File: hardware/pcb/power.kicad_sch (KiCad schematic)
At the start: 74 parts, among them J1 XT30PW-F, J12 Solar, J13 USB-C, Q3 AO3407, Q4 BSS123, Q5 AO3407, U1 AP63203WU, U11 USBLC6, U12 IP2326, U7 CN3722, U8 MT3608B

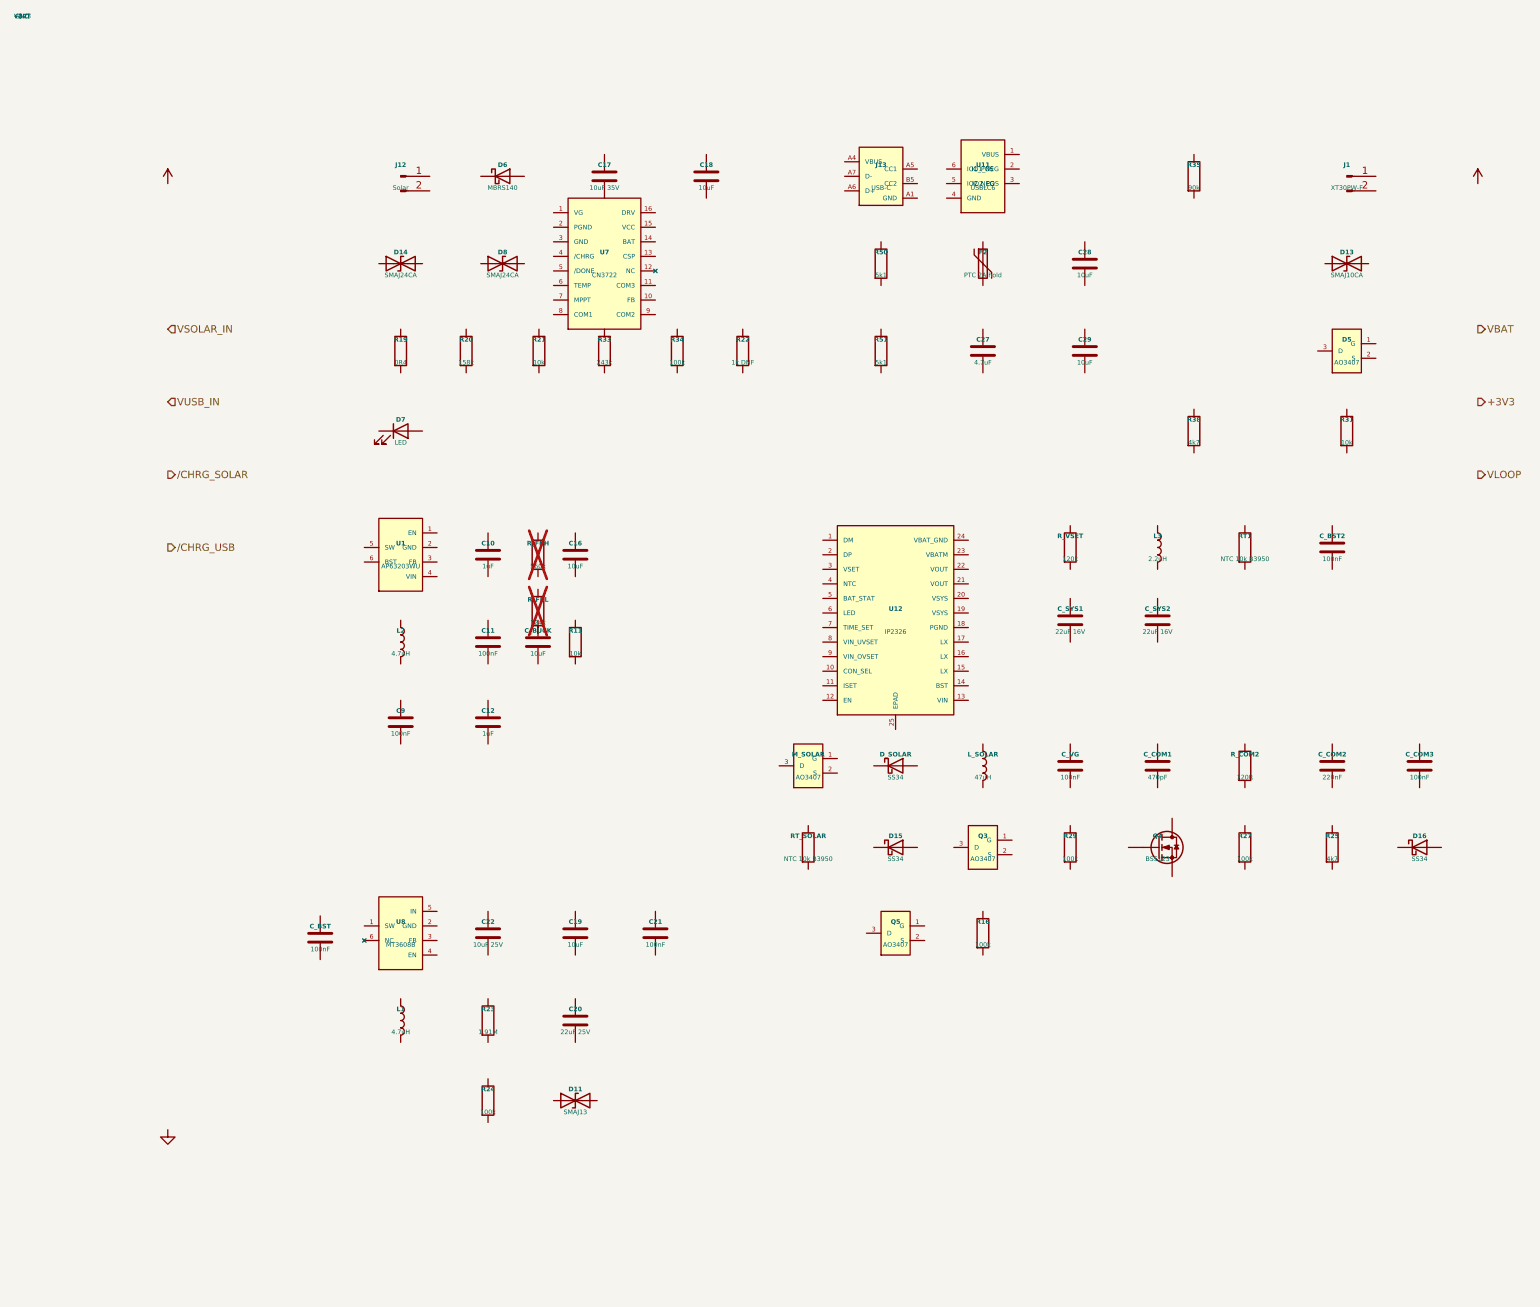
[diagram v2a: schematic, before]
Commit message: hw(pcb): wiring pass — schematic fully wired, netlist machine-verified (0 mismatches)
All four sheets wired with stub+label connectivity (434 wires, 21
explicit no-connects, PWR_FLAGs on undriven rails): power rails on
global labels, cross-sheet signals on hierarchical labels + rebuilt
top-sheet pins (24 hierarchical nets; vestigial ADC_CH* pins deleted,
GPIO14_LED corrected to the mcu-local net it really is), sheet-local
nets on local labels.

Verification (kicad-cli for the KiCad-10 format is not installable
here): hardware/pcb/kicad_wire_script.py generates the connectivity
from an embedded intent table derived from schematic_connections.md;
hardware/pcb/netlist_check.py independently re-extracts pin->net
geometrically (union-find over wires/labels/sheet pins) and diffs —
395 pins, 77 nets, 0 mismatches (output committed). Native KiCad 10
ERC + resave queued for the first interactive open.

Notable resolutions (recorded as design change #17): AP63203 FB tied
to +3V3 with the DNP divider floated at its midpoint; MT3608B pin 6
etype relaxed to passive so C_BST wiring is ERC-legal; IP2326 DM/DP
floated with no-connects (adapter detection is a two-wire future
change); D11 oriented cathode-to-VLOOP; decorative corner power
symbols replaced with real rail connectivity.

placement_constraints.md: Group G rewritten for the IP2326 hot loop,
new Group L for the CN3722 external buck (Kelvin CSP/BAT pair).
Top remaining risk flagged in blockers: AP63203 BST is NC per the
wiring doc but the AP6320x family likely requires a BST-SW cap —
resolve before layout freeze.

Co-Authored-By: Claude Fable 5 <noreply@anthropic.com>
Claude-Session: https://claude.ai/code/session_01VtMFY5Q94iYbsNPpLcPJyK
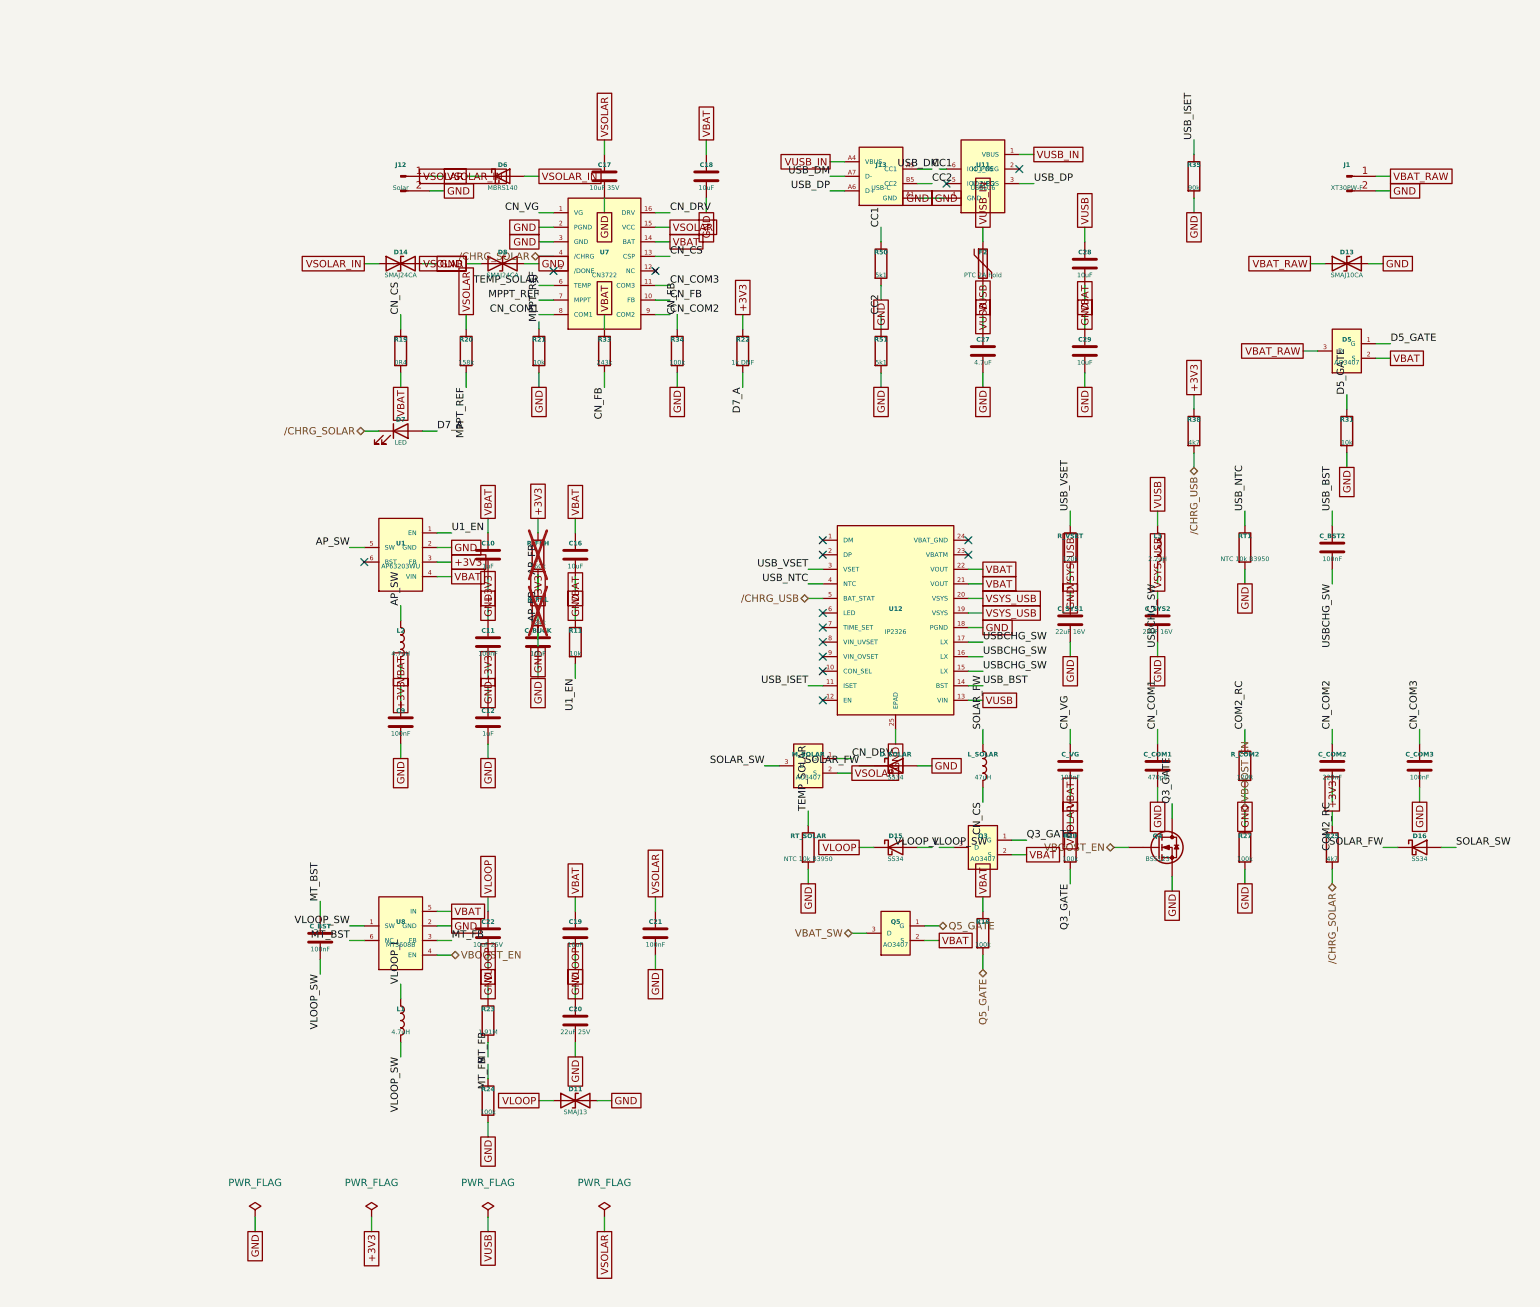
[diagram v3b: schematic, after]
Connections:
- net +3V3: now also C11.1, C12.1, C_BUCK.1, L2.2, R22.1, R25.1, R38.1, R_FBH.1, U1.3 (FB)
- net /CHRG_SOLAR: now also D7.1 (K), R25.2, U7.4 (/CHRG)
- net /CHRG_USB: now also R38.2, U12.5 (BAT_STAT)
- net GND: now also C10.2, C11.2, C12.2, C16.2, C17.2, C18.2, C19.2, C20.2, C21.2, C22.2, C27.2, C28.2, C29.2, C9.2, C_BUCK.2, C_COM1.2, C_COM3.2, C_SYS1.2, C_SYS2.2, D11.2 (A2), D13.2 (A2), D14.2 (A2), D8.2 (A2), D_SOLAR.2 (A), J1.2 (Pin_2), J12.2 (Pin_2), J13.A1 (GND), Q4.S, R21.2, R24.2, R27.2, R31.2, R34.2, R35.2, R50.2, R51.2, RT1.2, RT_SOLAR.2, R_COM2.2, R_FBL.2, R_VSET.2, U1.2 (GND), U11.4 (GND), U12.18 (PGND), U12.25 (EPAD), U7.2 (PGND), U7.3 (GND), U8.2 (GND)
- net VBAT: now also C10.1, C16.1, C18.1, C19.1, C29.1, C9.1, D5.2 (S), Q3.2 (S), Q5.2 (S), R11.1, R16.1, R19.2, R29.1, R33.1, U1.4 (VIN), U12.21 (VOUT), U12.22 (VOUT), U7.14 (BAT), U8.5 (IN)
- net VLOOP: now also C20.1, C22.1, D11.1 (A1), D15.1 (K), R23.1
- net VSOLAR_IN: now also D14.1 (A1), D6.2 (A), J12.1 (Pin_1)
- net VUSB_IN: now also F2.1, J13.A4 (VBUS), U11.1 (VBUS)
- net AP_SW: now reaches L2.1
- net AP_SW: now also U1.5 (SW)
- net CN_FB: now reaches R34.1
- net CN_FB: now also R33.2, U7.10 (FB)
- net MT_FB: now reaches R24.1
- net MT_FB: now also R23.2, U8.3 (FB)
- net VLOOP_SW: now reaches D15.2 (A)
- net VLOOP_SW: now also C_BST.2, L1.2, U8.1 (SW)
- net VUSB: now reaches C28.1
- net VUSB: now also C27.1, F2.2, L3.1, U12.13 (VIN)
- net TEMP_SOLAR: now reaches RT_SOLAR.1
- net TEMP_SOLAR: now also U7.6 (TEMP)
- net VBOOST_EN: now reaches U8.4 (EN)
- net VBOOST_EN: now also Q4.G, R27.1
- net MT_BST: now reaches U8.6 (NC)
- net MT_BST: now also C_BST.1
- net USBCHG_SW: now reaches L3.2
- net USBCHG_SW: now also C_BST2.2, U12.15 (LX), U12.16 (LX), U12.17 (LX)
- net VSOLAR: now reaches R20.1
- net VSOLAR: now also C17.1, C21.1, C_VG.2, D6.1 (K), D8.1 (A1), M_SOLAR.2 (S), U7.15 (VCC)
- net MPPT_REF: now reaches R20.2
- net MPPT_REF: now also R21.1, U7.7 (MPPT)
- net VLOOP_L: now reaches L1.1
- net VLOOP_L: now also Q3.3 (D)
- net USB_NTC: now reaches RT1.1
- net USB_NTC: now also U12.4 (NTC)
- net VSYS_USB: now reaches C_SYS2.1
- net VSYS_USB: now also C_SYS1.1, U12.19 (VSYS), U12.20 (VSYS)
- net USB_ISET: now reaches R35.1
- net USB_ISET: now also U12.11 (ISET)
- net CC2: now reaches R51.1
- net CC2: now also J13.B5 (CC2)
- net U1_EN: now reaches U1.1 (EN)
- net U1_EN: now also R11.2
- net CC1: now reaches R50.1
- net CC1: now also J13.A5 (CC1)
- net USB_DP: now reaches U11.3 (IO2_POS)
- net USB_DP: now also J13.A6 (D+)
- net USB_DM: now reaches U11.6 (IO1_POS)
- net USB_DM: now also J13.A7 (D-)
- net USB_VSET: now reaches R_VSET.1
- net USB_VSET: now also U12.3 (VSET)
- net USB_BST: now reaches C_BST2.1
- net USB_BST: now also U12.14 (BST)
- net CN_COM1: now reaches C_COM1.1
- net CN_COM1: now also U7.8 (COM1)
- net SOLAR_FW: now reaches D_SOLAR.1 (K)
- net SOLAR_FW: now also D16.1 (K), L_SOLAR.1
- net D5_GATE: now reaches R31.1
- net D5_GATE: now also D5.1 (G)
- net CN_VG: now reaches U7.1 (VG)
- net CN_VG: now also C_VG.1
- net CN_COM3: now reaches U7.11 (COM3)
- net CN_COM3: now also C_COM3.1
- net CN_CS: now reaches U7.13 (CSP)
- net CN_CS: now also L_SOLAR.2, R19.1
- net CN_DRV: now reaches U7.16 (DRV)
- net CN_DRV: now also M_SOLAR.1 (G)
- net CN_COM2: now reaches U7.9 (COM2)
- net CN_COM2: now also C_COM2.1
- net VBAT_RAW: now reaches D5.3 (D)
- net VBAT_RAW: now also D13.1 (A1), J1.1 (Pin_1)
- net COM2_RC: now reaches R_COM2.1
- net COM2_RC: now also C_COM2.2
- net Q3_GATE: now reaches Q4.D
- net Q3_GATE: now also Q3.1 (G), R29.2
- net SOLAR_SW: now reaches D16.2 (A)
- net SOLAR_SW: now also M_SOLAR.3 (D)
- net D7_A: now reaches D7.2 (A)
- net D7_A: now also R22.2
- net Q5_GATE: now reaches Q5.1 (G)
- net Q5_GATE: now also R16.2
- net VBAT_SW: now reaches Q5.3 (D)
- net AP_FB: now reaches R_FBH.2
- net AP_FB: now also R_FBL.1
- no-connect marks 0 -> 15
